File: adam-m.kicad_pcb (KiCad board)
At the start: 2 copper layers, 114.5 x 95.3 mm, 21 parts, among them J1 AudioJack4dpb, SW1 SW_Push, SW10 SW_Push, SW11 SW_Push, SW12 SW_Push, SW13 SW_Push, SW14 SW_Push, SW15 SW_Push, SW16 SW_Push, SW17 SW_Push, SW2 SW_Push, SW3 SW_Push, SW4 SW_Push, SW5 SW_Push, SW6 SW_Push, SW7 SW_Push, SW8 SW_Push, SW9 SW_Push, U1 ProMicro-kbd

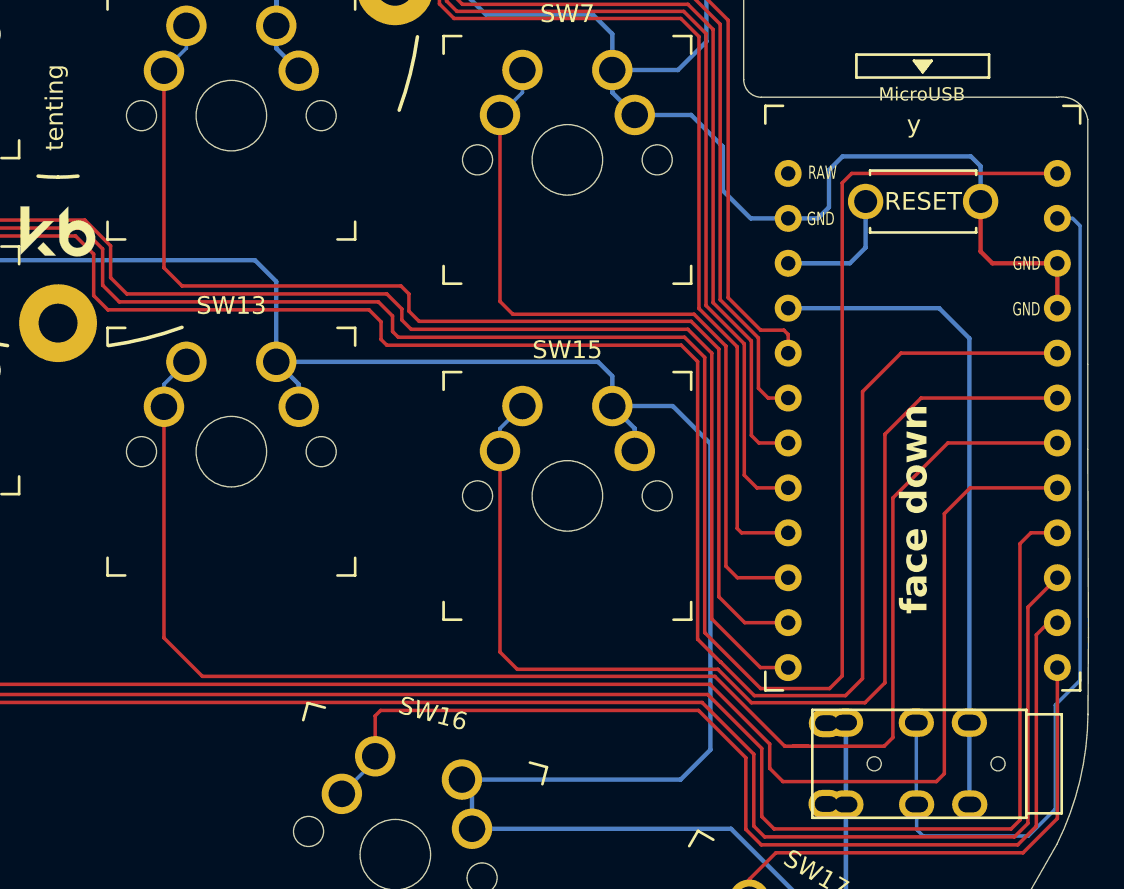
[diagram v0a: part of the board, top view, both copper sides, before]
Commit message: fix footprint for mcu
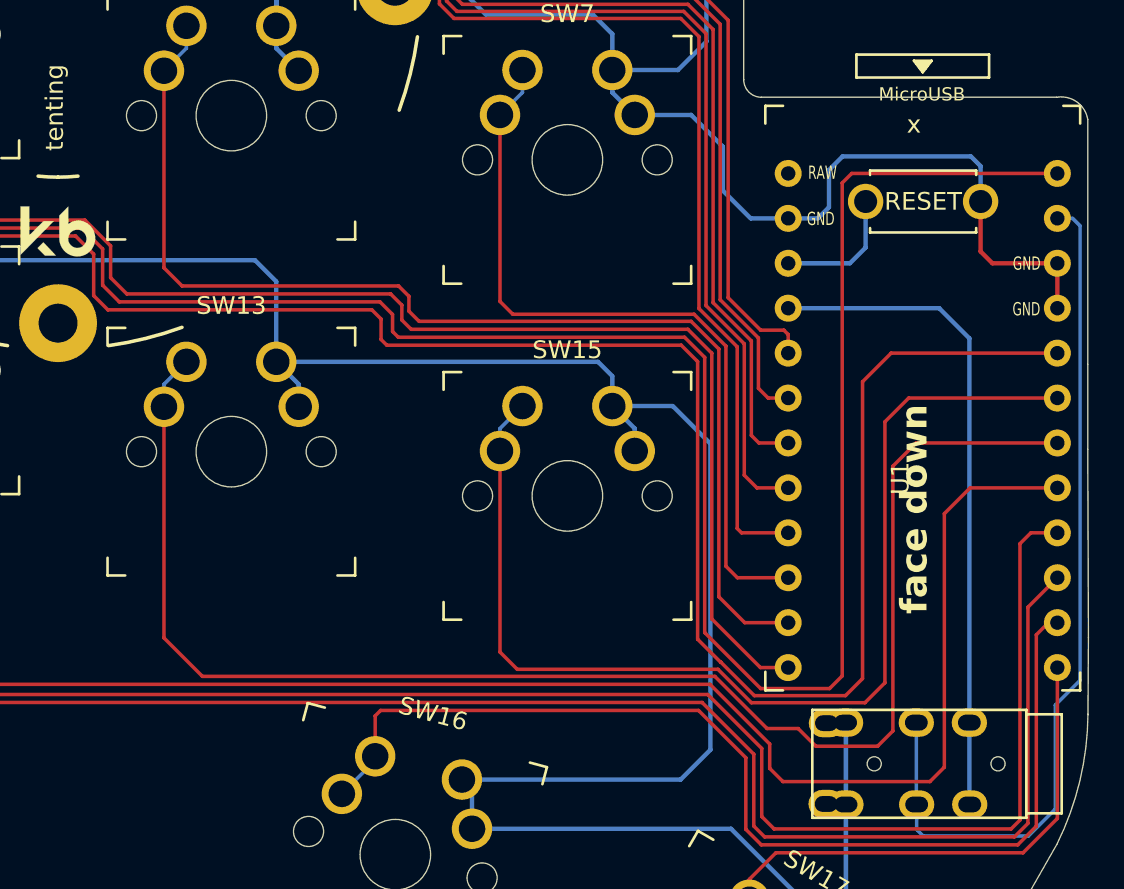
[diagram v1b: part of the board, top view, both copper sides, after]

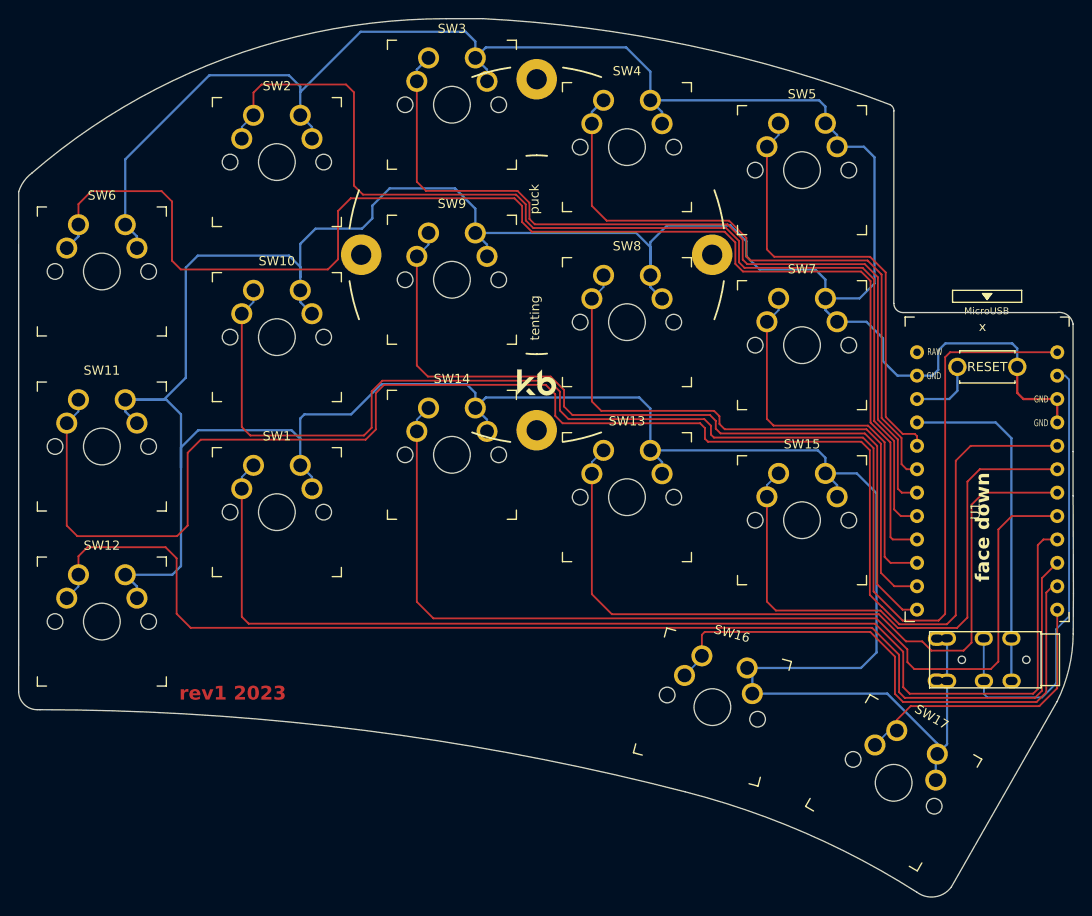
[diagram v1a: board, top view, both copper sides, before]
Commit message: Tweaks for ERC
- Removed silkscreen from pads of microcontroller, switch
- Moved trace closest to board edge to under microcontroller
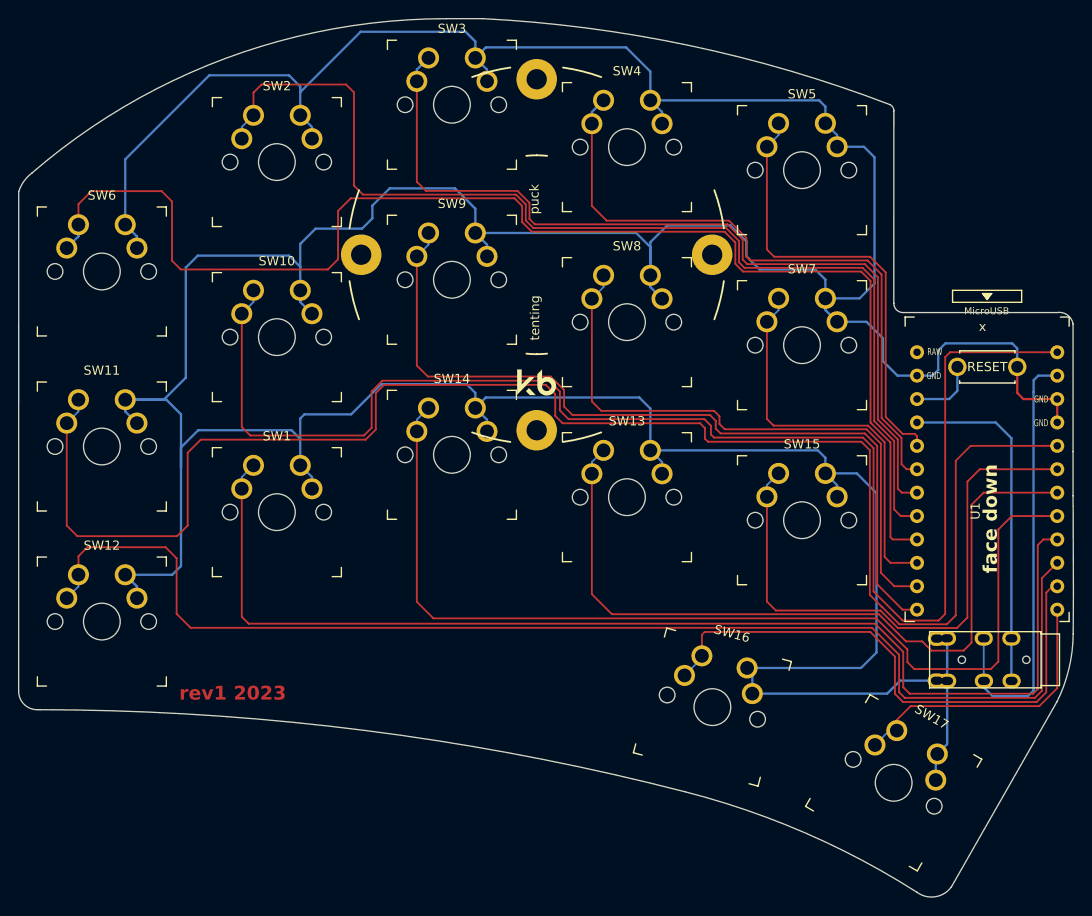
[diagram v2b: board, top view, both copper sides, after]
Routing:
- net gnd: track 526.2 -> 522.5 mm
- net Switch18: track 49.7 -> 47.8 mm

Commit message: update
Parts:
- U1: value ProMicro-kbd -> ProMicro-pinout
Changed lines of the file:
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@@
         (effects (font (size 1 1) (thickness 0.15)))
     )
-    (fp_text value "ProMicro-kbd" (at -1.27 14.732) (layer "F.Fab")
-        (effects (font (size 1 1) (thickness 0.15)))
+    (fp_text value "ProMicro-pinout" (at -0.6 13.4) (layer "F.SilkS")
+        (effects (font (size 0.75 0.75) (thickness 0.15)))
+    )
+    (fp_text user "GND" (at -5.77 -11.88) (layer "B.SilkS")
+        (effects (font (size 0.75 0.5) (thickness 0.125)) (justify mirror))
+    )
+    (fp_text user "GND" (at 5.88 -9.35) (layer "B.SilkS")
+        (effects (font (size 0.75 0.5) (thickness 0.125)) (justify mirror))
     )
     (fp_text user "GND" (at 5.86 -6.77) (layer "B.SilkS")
-        (effects (font (size 0.75 0.5) (thickness 0.125)) (justify mirror))
-    )
-    (fp_text user "GND" (at -5.77 -11.88) (layer "B.SilkS")
         (effects (font (size 0.75 0.5) (thickness 0.125)) (justify mirror))
     )
@@
         (effects (font (size 0.75 0.5) (thickness 0.125)) (justify mirror))
     )
-    (fp_text user "x" (at -1.2065 -16.256) (layer "B.SilkS")
-        (effects (font (size 1 1) (thickness 0.15)) (justify mirror))
-    )
-    (fp_text user "GND" (at 5.88 -9.35) (layer "B.SilkS")
-        (effects (font (size 0.75 0.5) (thickness 0.125)) (justify mirror))
-    )
-    (fp_text user "MicroUSB" (at -0.05 -18.95) (layer "F.SilkS")
-        (effects (font (size 0.75 0.75) (thickness 0.12)))
-    )
-    (fp_text user "x" (at -0.5 -17.25) (layer "F.SilkS")
-        (effects (font (size 1 1) (thickness 0.15)))
+    (fp_text user "GND" (at 5.86 -6.8) (layer "F.SilkS")
+        (effects (font (size 0.75 0.5) (thickness 0.125)))
     )
     (fp_text user "GND" (at -5.77 -11.91) (layer "F.SilkS")
-        (effects (font (size 0.75 0.5) (thickness 0.125)))
-    )
-    (fp_text user "RAW" (at -5.67 -14.52) (layer "F.SilkS")
         (effects (font (size 0.75 0.5) (thickness 0.125)))
     )
@@
         (effects (font (size 0.75 0.5) (thickness 0.125)))
     )
-    (fp_text user "GND" (at 5.86 -6.8) (layer "F.SilkS")
+    (fp_text user "RAW" (at -5.67 -14.52) (layer "F.SilkS")
         (effects (font (size 0.75 0.5) (thickness 0.125)))
     )
@@
       (stroke (width 0.15) (type solid)) (layer "F.SilkS"))
     (fp_line (start -8.9 14.75) (end -7.9 14.75)
-      (stroke (width 0.15) (type solid)) (layer "F.SilkS"))
-    (fp_line (start -3.75 -21.2) (end -3.75 -19.9)
-      (stroke (width 0.15) (type solid)) (layer "F.SilkS"))
-    (fp_line (start -3.75 -19.9) (end 3.75 -19.9)
-      (stroke (width 0.15) (type solid)) (layer "F.SilkS"))
-    (fp_line (start -0.5 -20.85) (end 0.5 -20.85)
-      (stroke (width 0.15) (type solid)) (layer "F.SilkS"))
-    (fp_line (start -0.35 -20.7) (end 0.35 -20.7)
-      (stroke (width 0.15) (type solid)) (layer "F.SilkS"))
-    (fp_line (start -0.25 -20.55) (end 0.25 -20.55)
-      (stroke (width 0.15) (type solid)) (layer "F.SilkS"))
-    (fp_line (start -0.15 -20.4) (end 0.15 -20.4)
-      (stroke (width 0.15) (type solid)) (layer "F.SilkS"))
-    (fp_line (start 0 -20.2) (end -0.5 -20.85)
-      (stroke (width 0.15) (type solid)) (layer "F.SilkS"))
-    (fp_line (start 0.5 -20.85) (end 0 -20.2)
-      (stroke (width 0.15) (type solid)) (layer "F.SilkS"))
-    (fp_line (start 3.75 -21.2) (end -3.75 -21.2)
-      (stroke (width 0.15) (type solid)) (layer "F.SilkS"))
-    (fp_line (start 3.75 -19.9) (end 3.75 -21.2)
       (stroke (width 0.15) (type solid)) (layer "F.SilkS"))
     (fp_line (start 8.9 -18.3) (end 7.95 -18.3)
@@
     (fp_line (start -8.9 14.75) (end -8.9 -18.3)
       (stroke (width 0.15) (type solid)) (layer "F.Fab"))
-    (fp_line (start -3.75 -19.6) (end -3.75 -18.299039)
-      (stroke (width 0.15) (type solid)) (layer "F.Fab"))
-    (fp_line (start -3.75 -19.6) (end 3.75 -19.6)
-      (stroke (width 0.15) (type solid)) (layer "F.Fab"))
     (fp_line (start -3.75 -18.3) (end 3.75 -18.3)
       (stroke (width 0.15) (type solid)) (layer "F.Fab"))
-    (fp_line (start 3.75 -19.6) (end 3.75 -18.3)
-      (stroke (width 0.15) (type solid)) (layer "F.Fab"))
     (fp_line (start 3.76 -18.3) (end 8.9 -18.3)

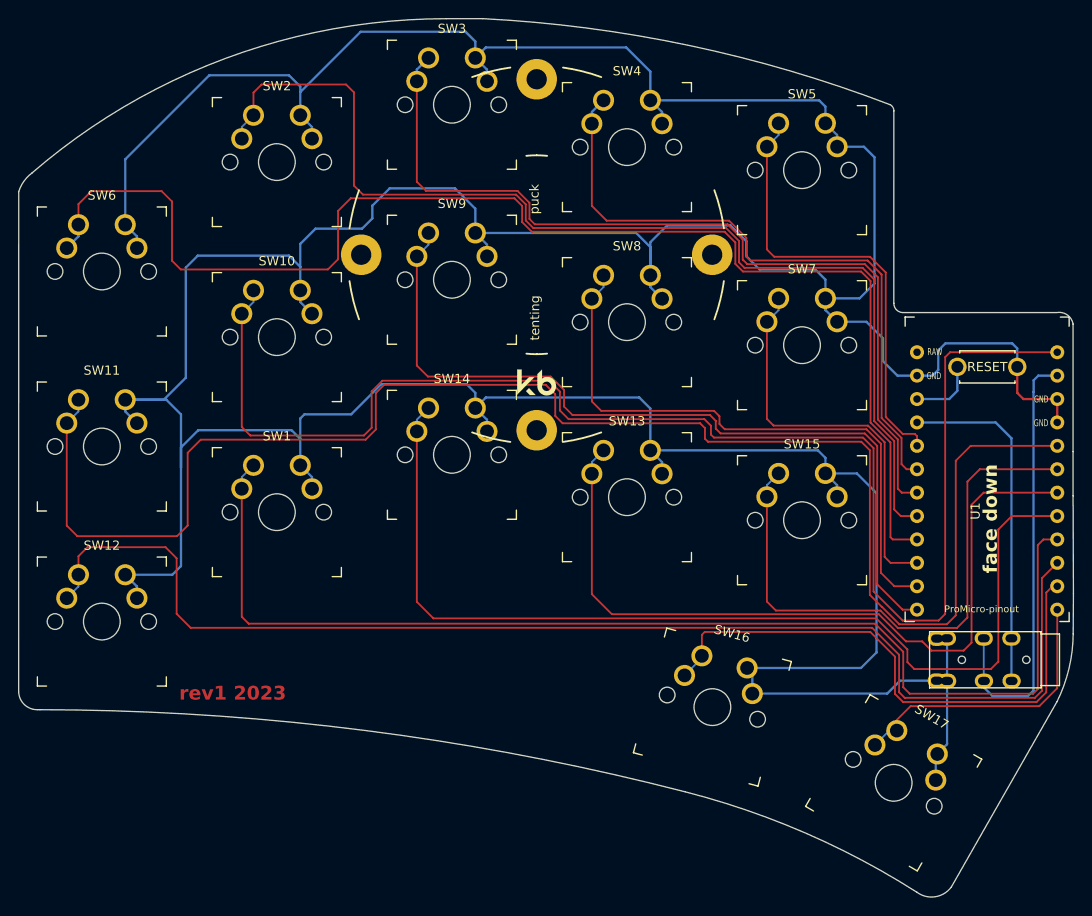
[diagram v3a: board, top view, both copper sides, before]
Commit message: more rounding, straighter lines, bit more text
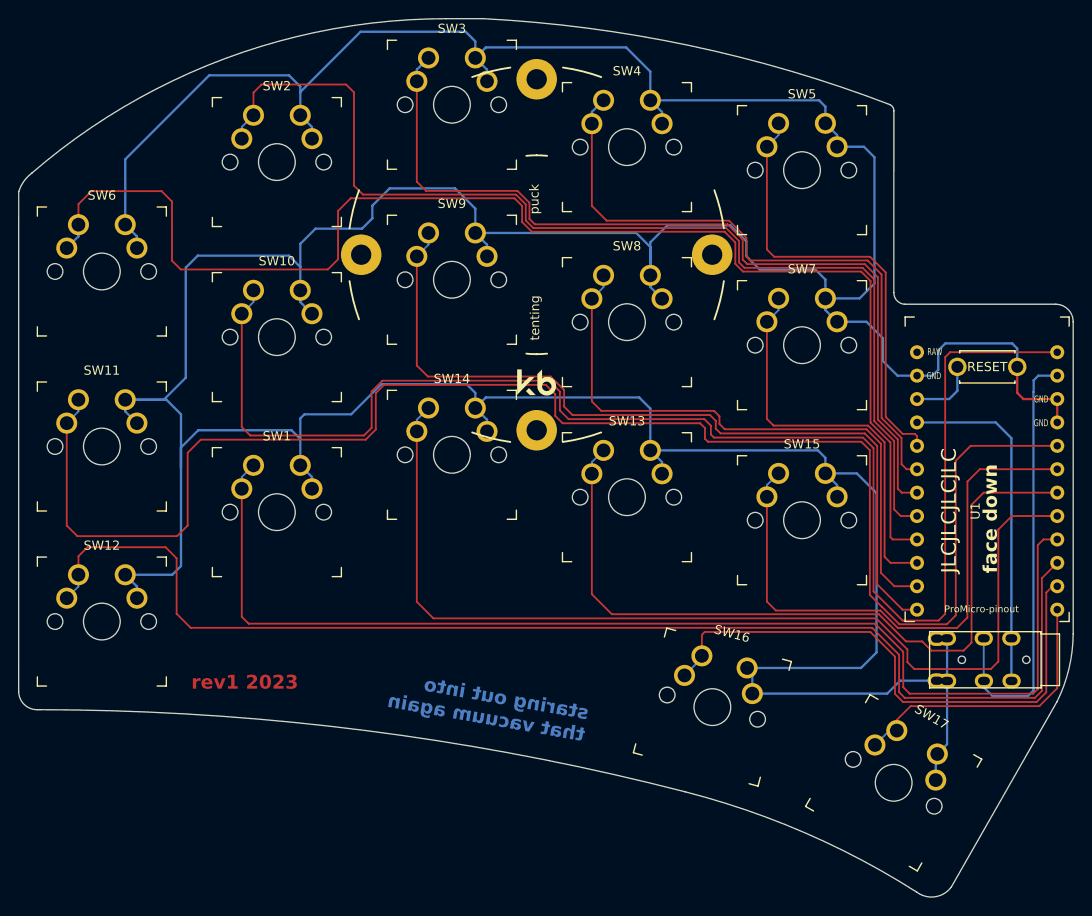
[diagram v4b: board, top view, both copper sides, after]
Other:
- outline, holes or cut-outs redrawn
- board text added: "JLCJLCJLCJLC"
- board text added: "staring out into that vacuum again"
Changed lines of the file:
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@@
   (gr_arc (start 189.83217 152.137949) (mid 188.091164 153.216421) (end 186.10017 152.736684)
-    (stroke (width 0.05) (type solid)) (layer "Edge.Cuts"))
-  (gr_line (start 203.03417 91.054684) (end 203.03417 104.888684)
     (stroke (width 0.05) (type solid)) (layer "Edge.Cuts"))
   (gr_arc (start 183.150415 67.231154) (mid 183.467204 67.50791) (end 183.58517 67.911684)
     (stroke (width 0.05) (type solid)) (layer "Edge.Cuts"))
+  (gr_line (start 201.14117 88.9) (end 184.785 88.9)
+    (stroke (width 0.05) (type default)) (layer "Edge.Cuts"))
   (gr_line (start 90.889706 132.915062) (end 90.615172 132.912601)
     (stroke (width 0.05) (type solid)) (layer "Edge.Cuts"))
-  (gr_line (start 203.07217 120.338684) (end 203.04617 124.686684)
+  (gr_line (start 203.04617 90.805) (end 203.04617 124.686684)
     (stroke (width 0.05) (type solid)) (layer "Edge.Cuts"))
   (gr_arc (start 90.615172 132.912601) (mid 89.202704 132.3634) (end 88.580171 130.981683)
     (stroke (width 0.05) (type solid)) (layer "Edge.Cuts"))
-  (gr_line (start 203.03417 109.700684) (end 203.07217 120.338684)
-    (stroke (width 0.05) (type solid)) (layer "Edge.Cuts"))
+  (gr_arc (start 201.14117 88.9) (mid 202.488208 89.457962) (end 203.04617 90.805)
+    (stroke (width 0.05) (type default)) (layer "Edge.Cuts"))
   (gr_arc (start 90.889711 132.912696) (mid 126.18485 135.166627) (end 160.919877 141.822821)
     (stroke (width 0.05) (type solid)) (layer "Edge.Cuts"))
@@
   (gr_line (start 88.588029 76.676004) (end 88.580171 130.981683)
     (stroke (width 0.05) (type solid)) (layer "Edge.Cuts"))
-  (gr_line (start 184.58017 89.804684) (end 201.28417 89.804684)
-    (stroke (width 0.05) (type solid)) (layer "Edge.Cuts"))
   (gr_arc (start 88.588029 76.676004) (mid 89.145373 75.558289) (end 90.016781 74.663545)
     (stroke (width 0.05) (type solid)) (layer "Edge.Cuts"))
   (gr_line (start 201.283849 132.052341) (end 189.83217 152.137949)
-    (stroke (width 0.05) (type solid)) (layer "Edge.Cuts"))
-  (gr_arc (start 201.28417 89.804684) (mid 202.418053 90.067247) (end 203.03417 91.054684)
     (stroke (width 0.05) (type solid)) (layer "Edge.Cuts"))
   (gr_arc (start 160.919877 141.822821) (mid 173.943392 146.279891) (end 186.10017 152.736684)
@@
   (gr_arc (start 90.016781 74.663545) (mid 110.993305 62.232) (end 134.99017 57.906684)
     (stroke (width 0.05) (type solid)) (layer "Edge.Cuts"))
-  (gr_line (start 203.03417 104.888684) (end 203.03417 109.700684)
-    (stroke (width 0.05) (type solid)) (layer "Edge.Cuts"))
   (gr_arc (start 203.04617 124.686684) (mid 202.585 128.47) (end 201.283849 132.052341)
     (stroke (width 0.05) (type solid)) (layer "Edge.Cuts"))
-  (gr_arc (start 184.58017 89.804684) (mid 183.873655 89.513261) (end 183.58017 88.807601)
+  (gr_arc (start 184.785 88.9) (mid 183.91956 88.514528) (end 183.58017 87.63)
+    (stroke (width 0.05) (type default)) (layer "Edge.Cuts"))
+  (gr_line (start 183.58017 87.63) (end 183.58517 67.911684)
     (stroke (width 0.05) (type solid)) (layer "Edge.Cuts"))
-  (gr_line (start 183.58017 88.807601) (end 183.58517 67.911684)
-    (stroke (width 0.05) (type solid)) (layer "Edge.Cuts"))
-  (gr_text "rev1 2023" (at 106 132) (layer "F.Cu")
+  (gr_text "rev1 2023" (at 107.315 130.81) (layer "F.Cu")
     (effects (font (size 1.5 1.5) (thickness 0.3) bold) (justify left bottom))
+  )
+  (gr_text "staring out into\nthat vacuum again" (at 149.86 136.525 350) (layer "B.Cu")
+    (effects (font (size 1.5 1.5) (thickness 0.3) bold) (justify left bottom mirror))
   )
   (gr_text "face up" (at 196.45 111.85 90) (layer "B.SilkS")
@@
     (effects (font (size 1.5 1.5) (thickness 0.3) bold) (justify left bottom))
   )
-  (gr_text "rev1 2023" (at 106 132) (layer "F.Mask")
+  (gr_text "JLCJLCJLCJLC" (at 190.5 118.11 90) (layer "F.SilkS")
+    (effects (font (size 1.6 1.6) (thickness 0.2)) (justify left bottom))
+  )
+  (gr_text "staring out into\nthat vacuum again" (at 149.86 136.525 350) (layer "B.Mask")
+    (effects (font (size 1.5 1.5) (thickness 0.3) bold) (justify left bottom mirror))
+  )
+  (gr_text "rev1 2023" (at 107.315 130.81) (layer "F.Mask")
     (effects (font (size 1.5 1.5) (thickness 0.3) bold) (justify left bottom))
   )
